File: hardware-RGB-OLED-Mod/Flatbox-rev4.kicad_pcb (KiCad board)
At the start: 2 copper layers, 210 x 124.5 mm, 68 parts, among them SW1 SW_Push, SW10 SW_Push, SW11 SW_Push, SW12 SW_Push, SW13 SW_Push, SW14 SW_Push, SW15 SW_Push, SW16 SW_Push, SW17 SW_Push, SW18 SW_Push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

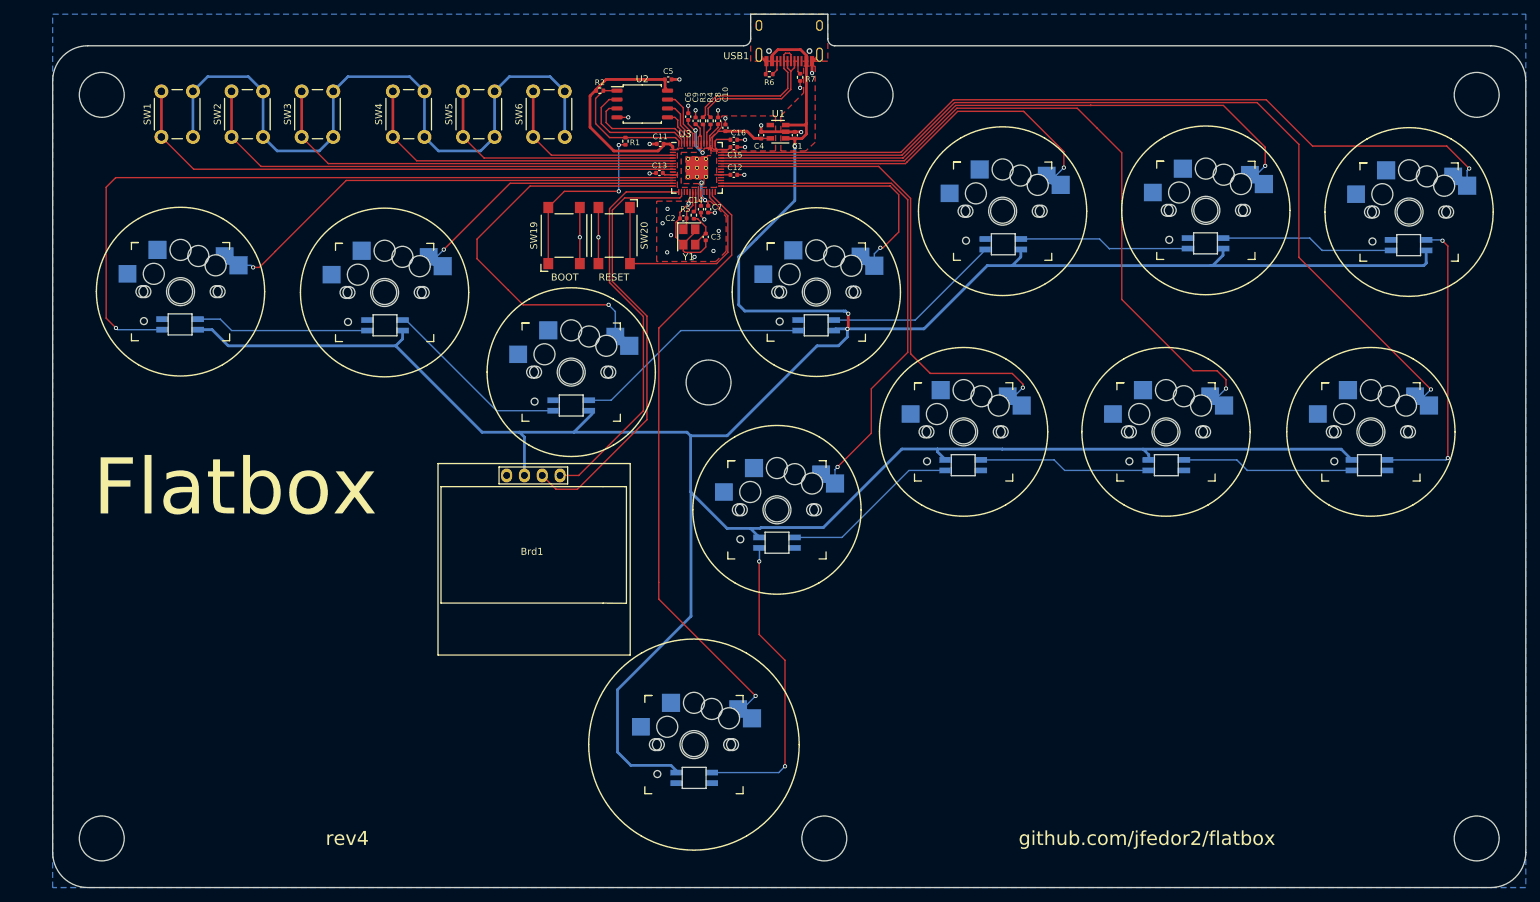
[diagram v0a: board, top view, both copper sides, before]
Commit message: Added Gerber files
Added Gerber files for production, PCBs on order from JLCPCB to confirm functionality.
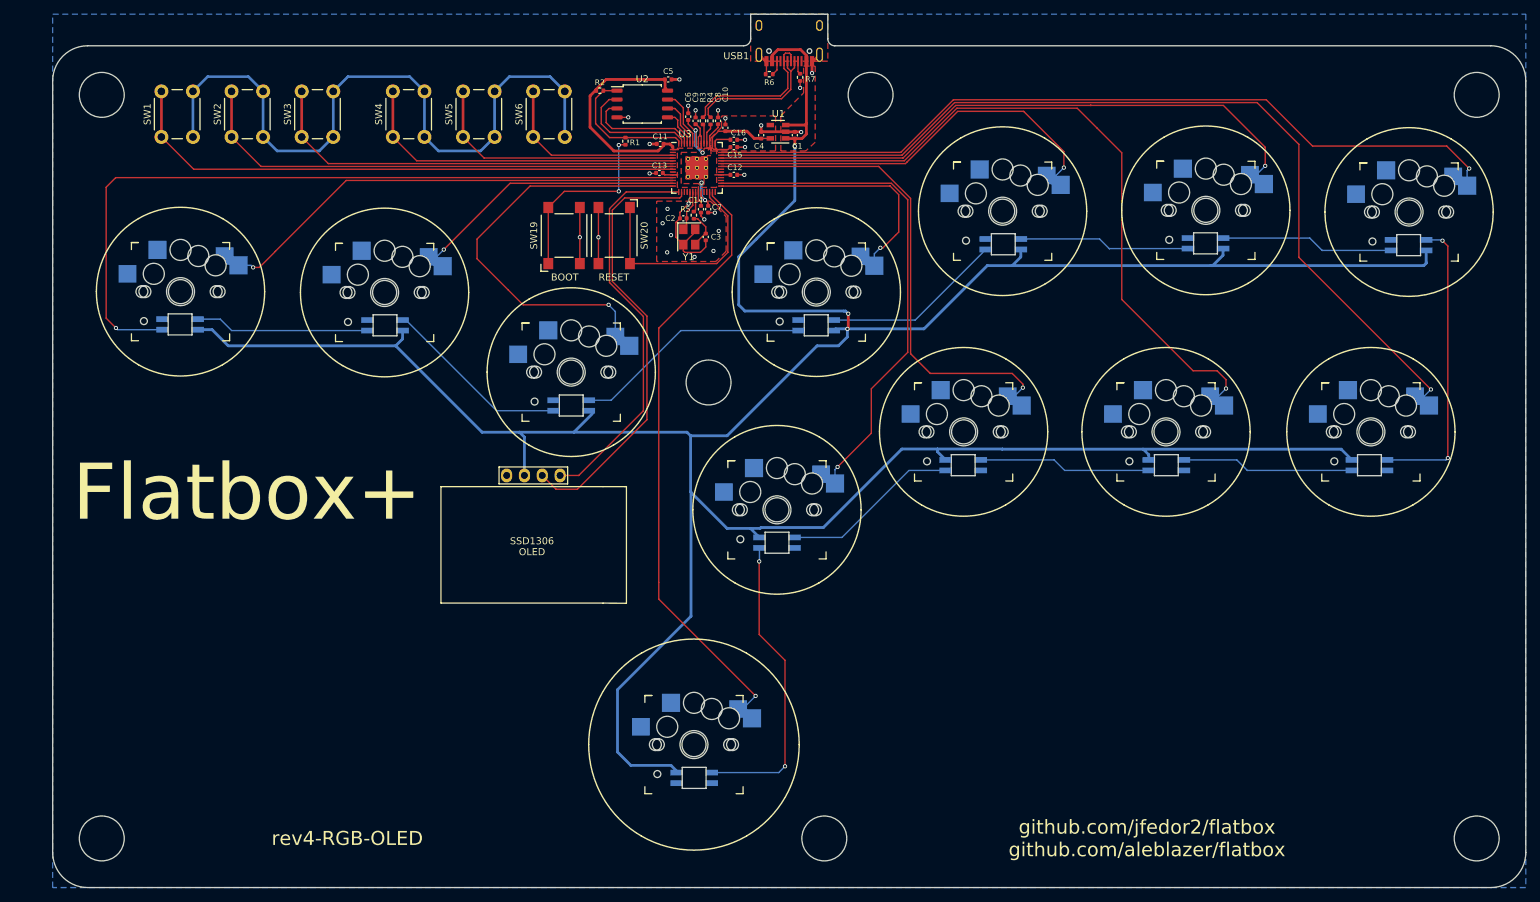
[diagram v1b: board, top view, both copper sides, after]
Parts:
- renumbered Brd1 to OLED
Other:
- board text added: "Flatbox+"
- board text added: "github.com/jfedor2/flatbox github.com/aleblazer/flatbox"
- board text added: "rev4-RGB-OLED"
- board text removed: "Flatbox"
- board text removed: "github.com/jfedor2/flatbox"
- board text removed: "rev4"
